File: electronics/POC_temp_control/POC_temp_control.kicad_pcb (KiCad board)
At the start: 2 copper layers, 109.2 x 78.7 mm, 47 parts, among them J1 Conn_01x02, J2 Conn_01x07, Q1 PXT8050, Q2 PXT8050, Q3 PXT8550, T1 10P_1P_2S, U1 SY8120, U2 MCP1702T-3302

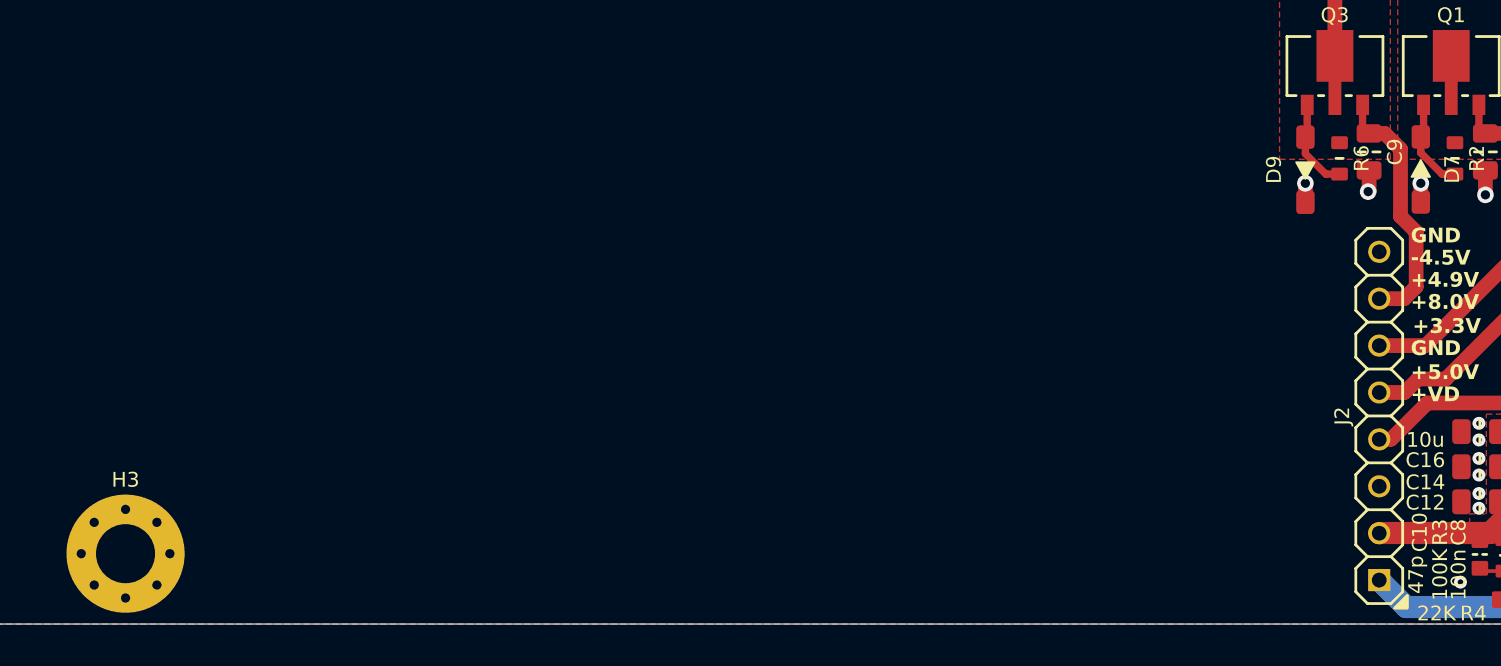
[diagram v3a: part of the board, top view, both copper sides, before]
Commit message: added nuclone footprint and component
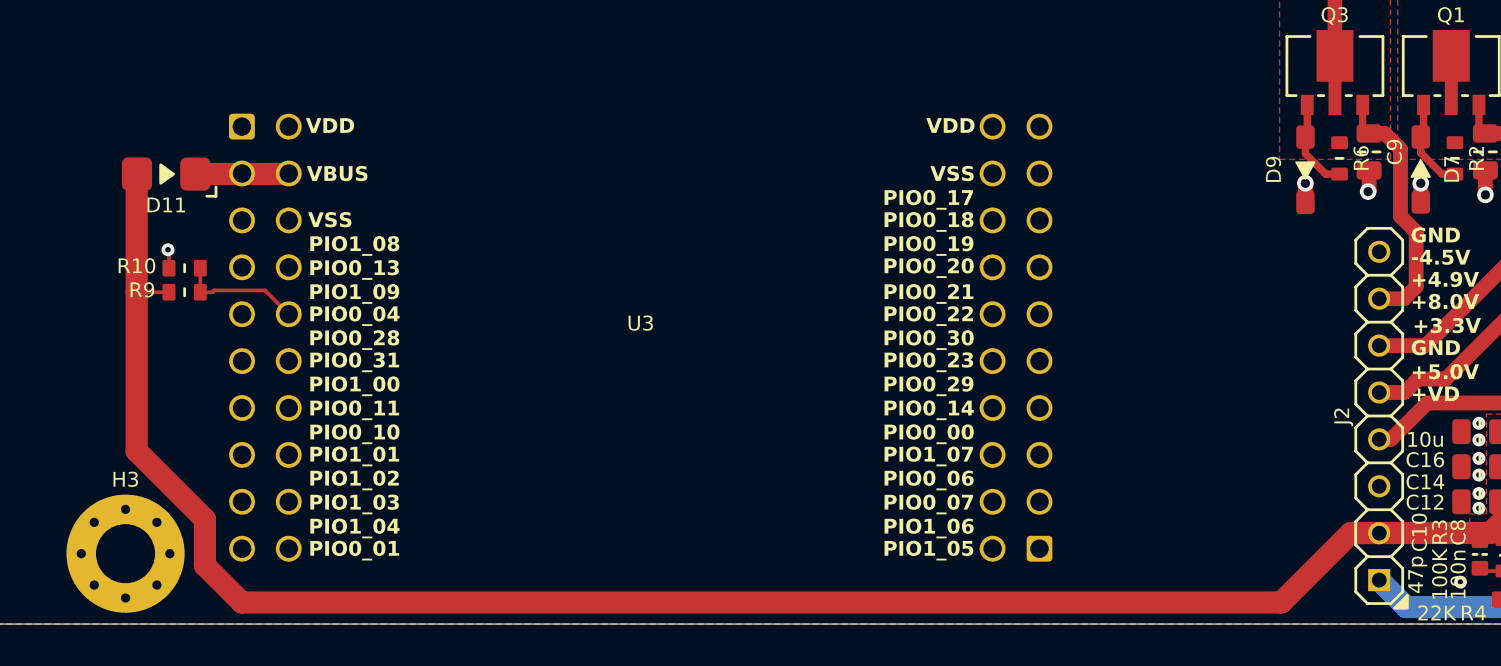
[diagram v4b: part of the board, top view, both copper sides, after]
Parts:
- added D11: D, SquantorDiodes:SOD-123F-hand, F.Cu at (40.3, 78.5)
- added R10: 10k, SquantorResistor:R_0603_hand, F.Cu at (41.3, 83.6)
- added R9: 5k6, SquantorResistor:R_0603_hand, F.Cu at (41.3, 84.9)
- added U3: ~, SquantorNuclone:nuclone_small_LPC845, F.Cu at (66.0, 87.0)
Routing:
- net /+5VD: track 10.9 -> 101.3 mm
- net /POWER_SENSE: track 0.00 -> 6.67 mm
- net /VBUS: track 0.00 -> 5.07 mm
- net /GND: track 14.8 -> 15.9 mm, vias 27 -> 28

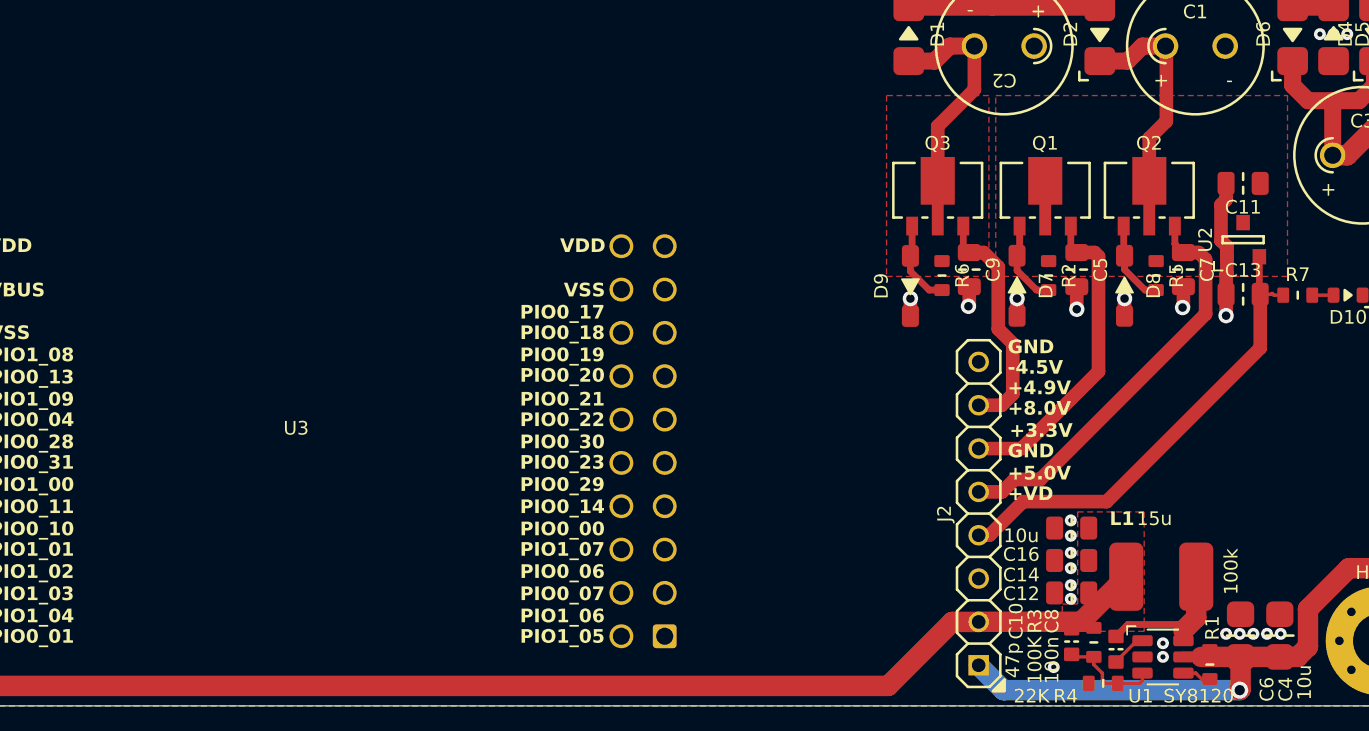
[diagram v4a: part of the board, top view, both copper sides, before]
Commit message: analog input filtering and post amps, started with diff amps
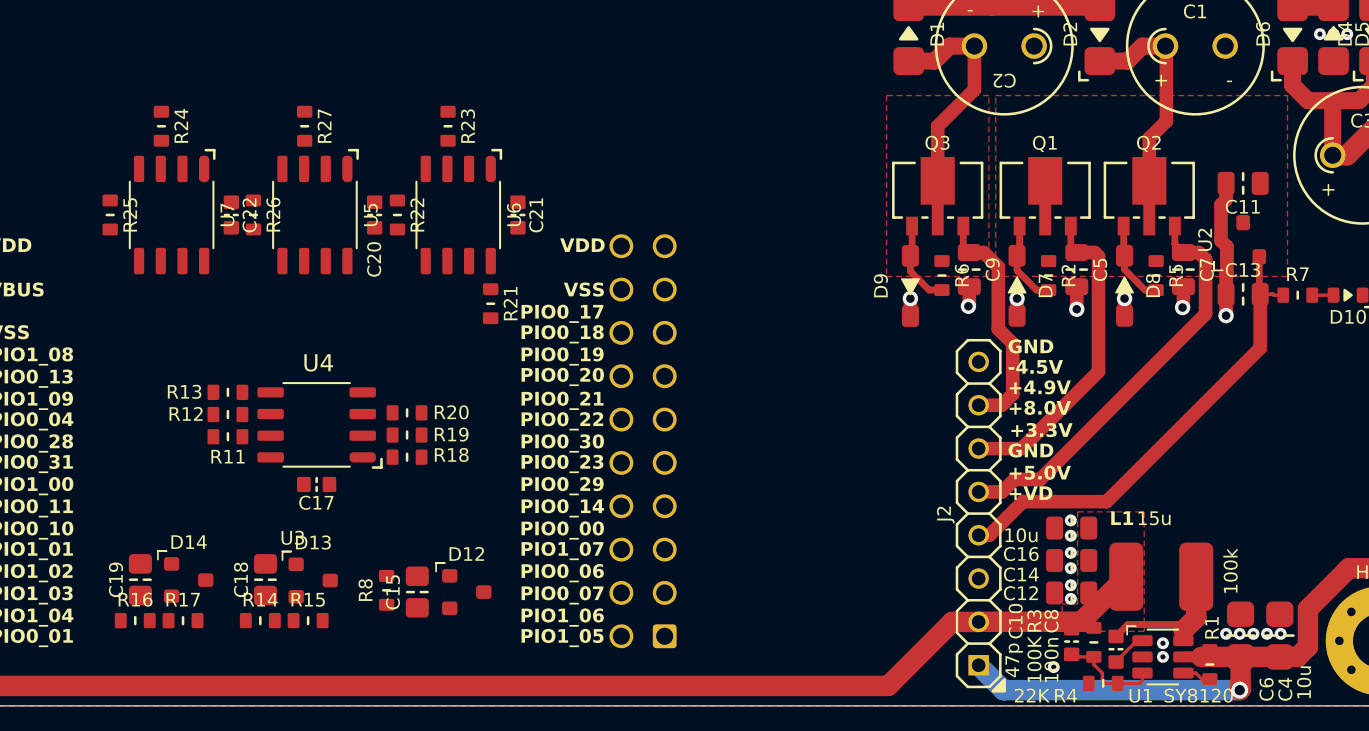
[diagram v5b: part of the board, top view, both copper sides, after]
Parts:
- added C15: 1u, SquantorCapacitor:C_0805+0603, F.Cu at (73.1, 96.2)
- added C17: 1u, SquantorCapacitor:C_0603, F.Cu at (67.2, 89.9)
- added C18: 1u, SquantorCapacitor:C_0805+0603, F.Cu at (64.2, 95.5)
- added C19: 1u, SquantorCapacitor:C_0805+0603, F.Cu at (56.9, 95.5)
- added C20: 1u, SquantorCapacitor:C_0603, F.Cu at (70.6, 74.1)
- added C21: 1u, SquantorCapacitor:C_0603, F.Cu at (79.0, 74.1)
- added C22: 1u, SquantorCapacitor:C_0603, F.Cu at (62.2, 74.1)
- added D12: ~, SquantorIC:SOT23-3, F.Cu at (76.0, 96.2)
- added D13: ~, SquantorIC:SOT23-3, F.Cu at (67.0, 95.5)
- added D14: ~, SquantorIC:SOT23-3, F.Cu at (59.7, 95.5)
- added R11: 22K6, SquantorResistor:R_0603_hand, F.Cu at (62.0, 87.1)
- added R12: 2K7, SquantorResistor:R_0603_hand, F.Cu at (62.0, 85.8)
- added R13: 2K7, SquantorResistor:R_0603_hand, F.Cu at (62.0, 84.5)
- added R14: 3K3, SquantorResistor:R_0603_hand, F.Cu at (63.9, 97.9)
- added R15: 3K3, SquantorResistor:R_0603_hand, F.Cu at (66.7, 97.9)
- added R16: 3K3, SquantorResistor:R_0603_hand, F.Cu at (56.6, 97.9)
- added R17: 3K3, SquantorResistor:R_0603_hand, F.Cu at (59.4, 97.9)
- added R18: 187K, SquantorResistor:R_0603_hand, F.Cu at (72.5, 88.3)
- added R19: 10K, SquantorResistor:R_0603_hand, F.Cu at (72.5, 87.0)
- added R20: 10K, SquantorResistor:R_0603_hand, F.Cu at (72.5, 85.7)
- added R21: 82K, SquantorResistor:R_0603_hand, F.Cu at (77.4, 79.3)
- added R22: 590K, SquantorResistor:R_0603_hand, F.Cu at (71.9, 74.1)
- added R23: 590K, SquantorResistor:R_0603_hand, F.Cu at (74.9, 68.9)
- added R24: 453K, SquantorResistor:R_0603_hand, F.Cu at (58.1, 68.9)
- added R25: 453K, SquantorResistor:R_0603_hand, F.Cu at (55.1, 74.1)
- added R26: 200K, SquantorResistor:R_0603_hand, F.Cu at (63.5, 74.1)
- added R27: 200K, SquantorResistor:R_0603_hand, F.Cu at (66.5, 68.9)
- added R8: 2K2, SquantorResistor:R_0603_hand, F.Cu at (71.3, 96.1)
- added U4: LM358, SquantorIC:SOIC-8, F.Cu at (67.2, 86.4)
- added U5: OP07, SquantorIC:SOIC-8, F.Cu at (67.1, 74.1)
- added U6: OP07, SquantorIC:SOIC-8, F.Cu at (75.5, 74.1)
- added U7: OP07, SquantorIC:SOIC-8, F.Cu at (58.7, 74.1)
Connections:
- U3 pad 24: unconnected-(U3B-PIO0_07-Pad24) -> /TC_FILT

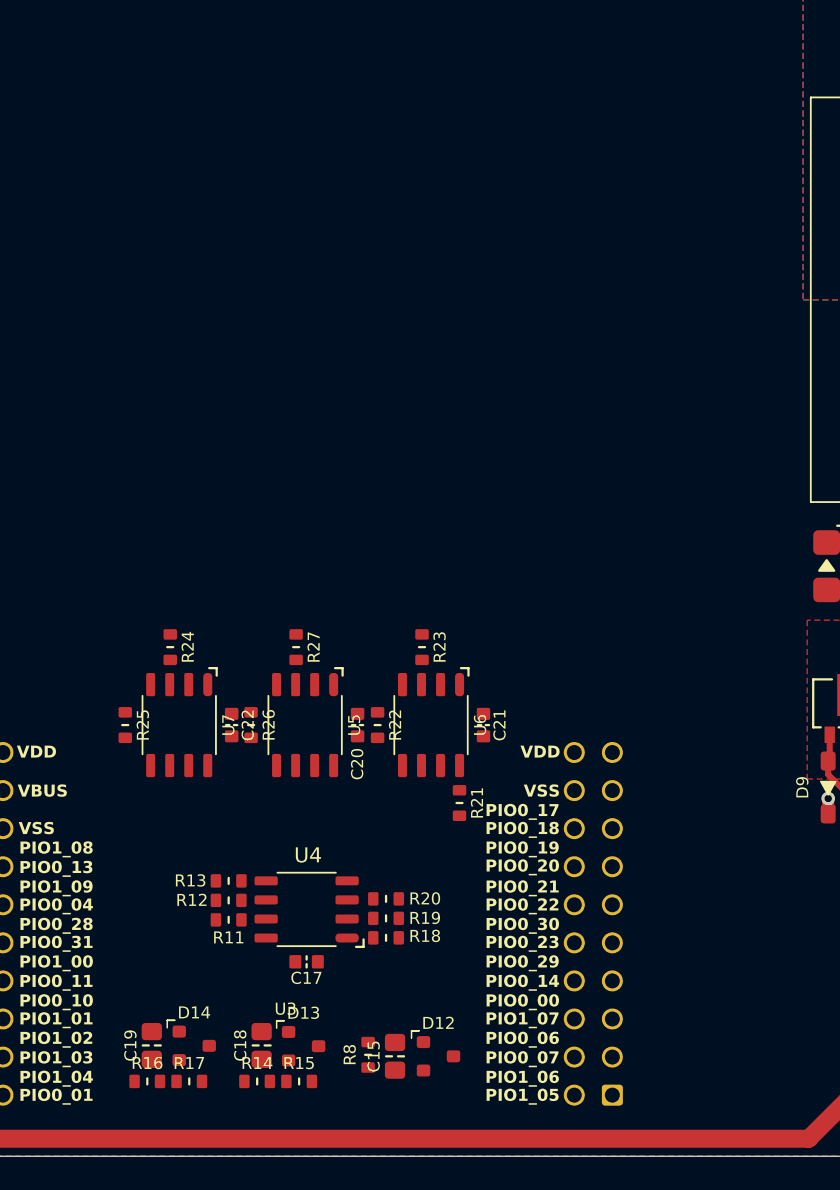
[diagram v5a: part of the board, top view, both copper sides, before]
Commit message: finished diff amp schematic and analog multiplexers
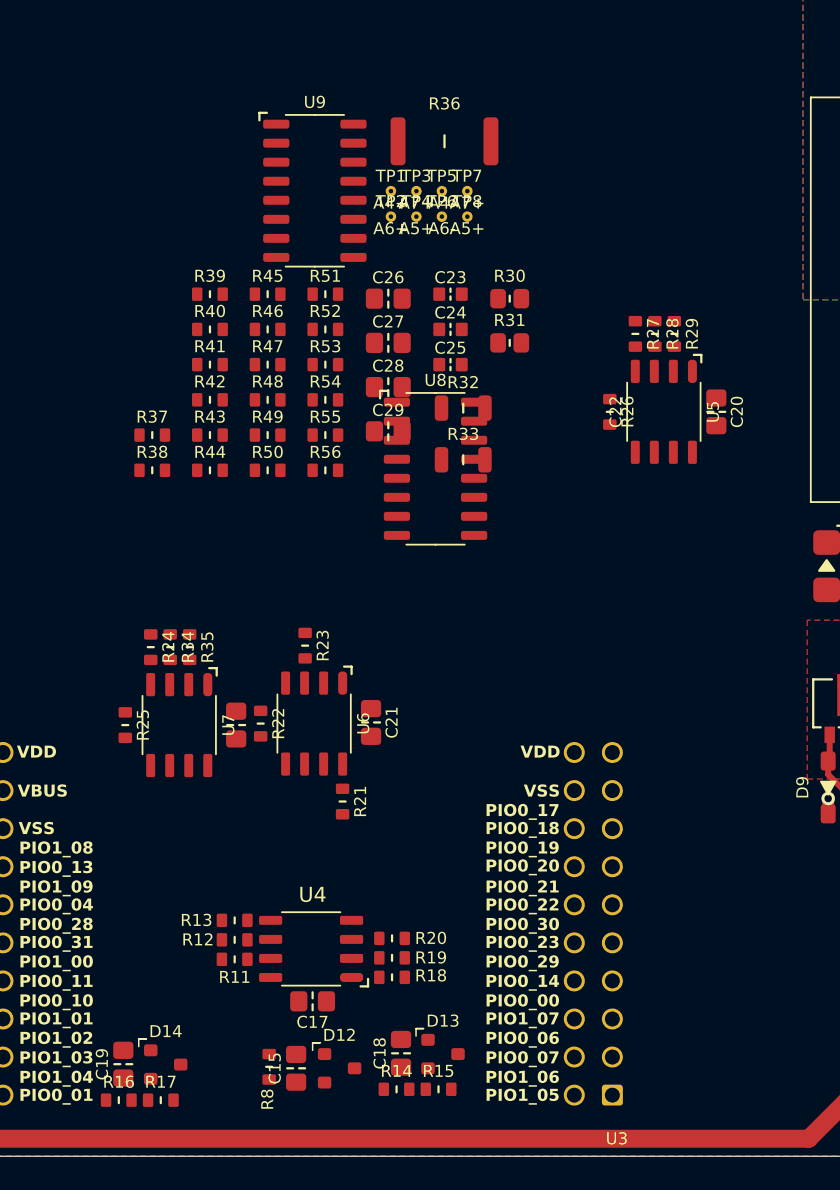
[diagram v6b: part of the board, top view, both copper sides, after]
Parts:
- added C23: 1u, SquantorCapacitor:C_0603, F.Cu at (76.8, 45.4)
- added C24: 1u, SquantorCapacitor:C_0603, F.Cu at (76.8, 47.7)
- added C25: 1u, SquantorCapacitor:C_0603, F.Cu at (76.8, 50.0)
- added C26: 1u, SquantorCapacitor:C_0805+0603, F.Cu at (72.7, 45.6)
- added C27: 1u, SquantorCapacitor:C_0805+0603, F.Cu at (72.7, 48.6)
- added C28: 1u, SquantorCapacitor:C_0805+0603, F.Cu at (72.7, 51.5)
- added C29: 1u, SquantorCapacitor:C_0805+0603, F.Cu at (72.7, 54.5)
- added R28: 4k75, SquantorResistor:R_0603_hand, F.Cu at (90.4, 48.0)
- added R29: 4k75, SquantorResistor:R_0603_hand, F.Cu at (91.7, 48.0)
- added R30: 0R22, SquantorResistor:R_0805+0603, F.Cu at (80.8, 45.6)
- added R31: 0R22, SquantorResistor:R_0805+0603, F.Cu at (80.8, 48.6)
- added R32: 1M, SquantorResistor:R_1206, F.Cu at (77.7, 53.0)
- added R33: 1A25, SquantorResistor:R_1206, F.Cu at (77.7, 56.4)
- added R34: 20K, SquantorResistor:R_0603_hand, F.Cu at (58.1, 68.9)
- added R35: 20K, SquantorResistor:R_0603_hand, F.Cu at (59.4, 68.9)
- added R36: R005, SquantorResistor:R_2512, F.Cu at (76.4, 35.1)
- added R37: 10K, SquantorResistor:R_0603_hand, F.Cu at (56.9, 54.8)
- added R38: 10K, SquantorResistor:R_0603_hand, F.Cu at (56.9, 57.1)
- added R39: 10K, SquantorResistor:R_0603_hand, F.Cu at (60.8, 45.4)
- added R40: 10K, SquantorResistor:R_0603_hand, F.Cu at (60.8, 47.7)
- added R41: 22K6, SquantorResistor:R_0603_hand, F.Cu at (60.8, 50.0)
- added R42: 22K6, SquantorResistor:R_0603_hand, F.Cu at (60.8, 52.4)
- added R43: 22K6, SquantorResistor:R_0603_hand, F.Cu at (60.8, 54.8)
- added R44: 22K6, SquantorResistor:R_0603_hand, F.Cu at (60.8, 57.1)
- added R45: 22K6, SquantorResistor:R_0603_hand, F.Cu at (64.6, 45.4)
- added R46: 22K6, SquantorResistor:R_0603_hand, F.Cu at (64.6, 47.7)
- added R47: 22K6, SquantorResistor:R_0603_hand, F.Cu at (64.6, 50.0)
- added R48: 22K6, SquantorResistor:R_0603_hand, F.Cu at (64.6, 52.4)
- added R49: 22K6, SquantorResistor:R_0603_hand, F.Cu at (64.6, 54.8)
- added R50: 22K6, SquantorResistor:R_0603_hand, F.Cu at (64.6, 57.1)
- added R51: 22K6, SquantorResistor:R_0603_hand, F.Cu at (68.5, 45.4)
- added R52: 22K6, SquantorResistor:R_0603_hand, F.Cu at (68.5, 47.7)
- added R53: 22K6, SquantorResistor:R_0603_hand, F.Cu at (68.5, 50.0)
- added R54: 22K6, SquantorResistor:R_0603_hand, F.Cu at (68.5, 52.4)
- added R55: 22K6, SquantorResistor:R_0603_hand, F.Cu at (68.5, 54.8)
- added R56: 22K6, SquantorResistor:R_0603_hand, F.Cu at (68.5, 57.1)
- added TP1: A4+, SquantorTestPoints:TestPoint_hole_H03R07, F.Cu at (72.8, 38.5)
- added TP2: A6+, SquantorTestPoints:TestPoint_hole_H03R07, F.Cu at (72.8, 40.2)
- added TP3: A7+, SquantorTestPoints:TestPoint_hole_H03R07, F.Cu at (74.5, 38.5)
- added TP4: A5+, SquantorTestPoints:TestPoint_hole_H03R07, F.Cu at (74.5, 40.2)
- added TP5: A4-, SquantorTestPoints:TestPoint_hole_H03R07, F.Cu at (76.2, 38.5)
- added TP6: A6-, SquantorTestPoints:TestPoint_hole_H03R07, F.Cu at (76.2, 40.2)
- added TP7: A7+, SquantorTestPoints:TestPoint_hole_H03R07, F.Cu at (77.9, 38.5)
- added TP8: A5+, SquantorTestPoints:TestPoint_hole_H03R07, F.Cu at (77.9, 40.2)
- added U8: 74XX4051, SquantorIC:SOIC-16_3.9x9.9mm_P1.27mm, F.Cu at (75.8, 57.0)
- added U9: 74XX4051, SquantorIC:SOIC-16_3.9x9.9mm_P1.27mm, F.Cu at (67.8, 38.5)
- C17, C20, C21, C22: footprint SquantorCapacitor:C_0603 -> SquantorCapacitor:C_0805+0603
- moved R26 31.8 mm to (87.4, 53.2)
- moved C20 31.8 mm to (94.5, 53.2)
- moved U5 31.8 mm to (91.0, 53.2)
- moved R27 30.8 mm to (89.1, 48.0)
- moved R14 9.31 mm to (73.2, 98.4)
- moved C18 9.31 mm to (73.5, 96.0)
- moved D13 9.31 mm to (76.3, 96.0)
- moved R15 9.31 mm to (76.0, 98.4)
- moved R21 7.80 mm to (69.6, 79.2)
- moved R23 7.80 mm to (67.1, 68.8)
- moved R22 7.80 mm to (64.1, 74.0)
- moved U6 7.80 mm to (67.7, 74.0)
- moved C21 7.50 mm to (71.5, 73.9)
- moved R8 6.65 mm to (64.7, 96.9)
- moved C15 6.65 mm to (66.5, 97.0)
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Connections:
- net Net-(U6-+IN) renamed /TC+DIFF
- net Net-(U6--IN) renamed /TC-DIFF
- U3 pad 13: unconnected-(U3A-PIO1_00-Pad13) -> /MUX_S0
- U3 pad 16: unconnected-(U3A-PIO1_01-Pad16) -> /MUX_S1
- U3 pad 17: unconnected-(U3A-PIO1_02-Pad17) -> /MUX_S2
- U3 pad 18: unconnected-(U3A-PIO1_03-Pad18) -> /MUX_EN

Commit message: WIP DIY soldering station
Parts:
- added C30: 1u, SquantorCapacitor:C_0805+0603, F.Cu at (53.8, 43.7)
- added D17: BZX84C18, SquantorIC:SOT23-3, F.Cu at (53.7, 46.5)
- added D18: BAS16, SquantorIC:SOT23-3, F.Cu at (54.1, 51.4)
- added D19: BAV79, SquantorIC:SOT23-3, F.Cu at (47.5, 44.6)
- added J3: Conn_01x05, Connector_JST:JST_XH_B5B-XH-A_1x05_P2.50mm_Vertical, F.Cu at (63.0, 27.0)
- added J4: Conn_01x06, Connector_JST:JST_XH_B6B-XH-A_1x06_P2.50mm_Vertical, F.Cu at (44.5, 27.0)
- added J5: Conn_01x02, SquantorPhoenixContact:MKDS_2conn_508pitch_1711725, F.Cu at (30.5, 40.6)
- added J6: Conn_01x02, SquantorPhoenixContact:MKDS_2conn_508pitch_1711725, F.Cu at (30.5, 29.6)
- added JP1: AC, SquantorSpecial:solder_jumper_3mm_SMD, F.Cu at (45.8, 36.8)
- added JP2: AC, SquantorSpecial:solder_jumper_3mm_SMD, F.Cu at (45.8, 40.4)
- added OP1: ~, SquantorOpto:OP_SOIC_4, F.Cu at (50.6, 50.6)
- added OP2: ~, SquantorOpto:OP_SOIC_4, F.Cu at (47.1, 50.6)
- added Q4: Q_PMOS_DUAL, SquantorIC:SOIC-8, F.Cu at (50.0, 38.9)
- added Q5: BC858B, SquantorIC:SOT23-3, F.Cu at (50.6, 56.6)
- added Q6: BC847A, SquantorIC:SOT23-3, F.Cu at (47.2, 56.6)
- added R57: 10M, SquantorResistor:R_0603_hand, F.Cu at (53.6, 38.8)
- added R58: 5K6, SquantorResistor:R_0603_hand, F.Cu at (50.6, 44.2)
- added R59: 1M, SquantorResistor:R_0603_hand, F.Cu at (45.1, 45.0)
- added R60: 2K2, SquantorResistor:R_0603_hand, F.Cu at (53.7, 49.0)
- added R61: 1K5, SquantorResistor:R_0603_hand, F.Cu at (50.6, 45.7)
- added R62: 330, SquantorResistor:R_0603_hand, F.Cu at (53.0, 54.5)
- added R63: 330, SquantorResistor:R_0603_hand, F.Cu at (44.8, 54.5)
- added R64: 10K, SquantorResistor:R_0603_hand, F.Cu at (48.8, 59.8)
- added R65: 10K, SquantorResistor:R_0603_hand, F.Cu at (50.9, 60.4)
- added R66: 10K, SquantorResistor:R_0603_hand, F.Cu at (47.5, 59.8)
- added R67: 6K8, SquantorResistor:R_0603_hand, F.Cu at (50.9, 59.1)
- C26, C27, C28, C29: footprint SquantorCapacitor:C_0805+0603 -> SquantorCapacitor:C_0603
- moved R26 71.6 mm to (26.4, 90.7)
- moved C20 71.6 mm to (33.5, 90.7)
- moved R27 71.6 mm to (28.1, 85.5)
- moved R28 71.6 mm to (29.4, 85.5)
- moved R29 71.6 mm to (30.7, 85.5)
- moved U5 71.6 mm to (30.0, 90.7)
- moved C23 58.5 mm to (30.9, 81.6)
- moved F1 54.6 mm to (27.6, 78.1)
- moved D11 54.2 mm to (91.7, 95.6), turned to 0 degrees
- moved R30 53.7 mm to (32.8, 69.9)
- moved R32 52.3 mm to (29.6, 73.6)
- moved R31 52.1 mm to (31.4, 65.3)
- moved R10 51.5 mm to (92.5, 89.0), turned to 180 degrees
- moved R9 51.3 mm to (92.5, 87.7), turned to 0 degrees
- moved R36 47.2 mm to (32.2, 51.6), turned to 180 degrees
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- renumbered R33 to F1
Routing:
- net /+5VD: track 101.3 -> 24.6 mm
- net /VD3.3V+: track 0.00 -> 49.5 mm
- net /POWER_SENSE: track 6.67 -> 0.00 mm
